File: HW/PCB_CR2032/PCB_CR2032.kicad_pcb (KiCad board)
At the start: 4 copper layers, 39.1 x 48 mm, 76 parts, among them J1 STDC14, J2 Breakoff, J3 PWR, M00 LED, M01 LED, M02 LED, M03 LED, M10 LED, M11 LED, M12 LED, M13 LED, SW1 WAKE, U1 STM32L071CBTx, U2 LIS3DH, Y1 32768 Hz

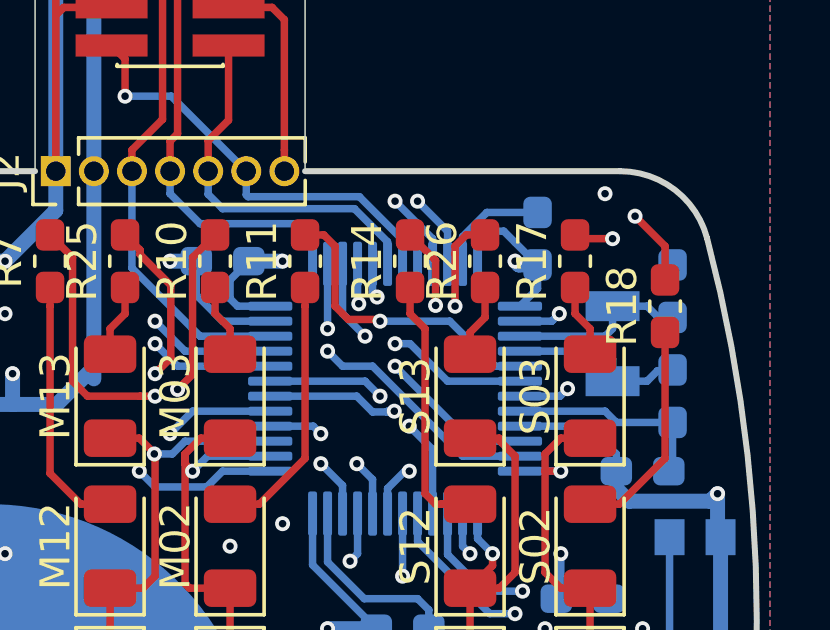
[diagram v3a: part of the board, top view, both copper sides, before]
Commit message: Connected BOOT0 pin to GND after forst board bring up.
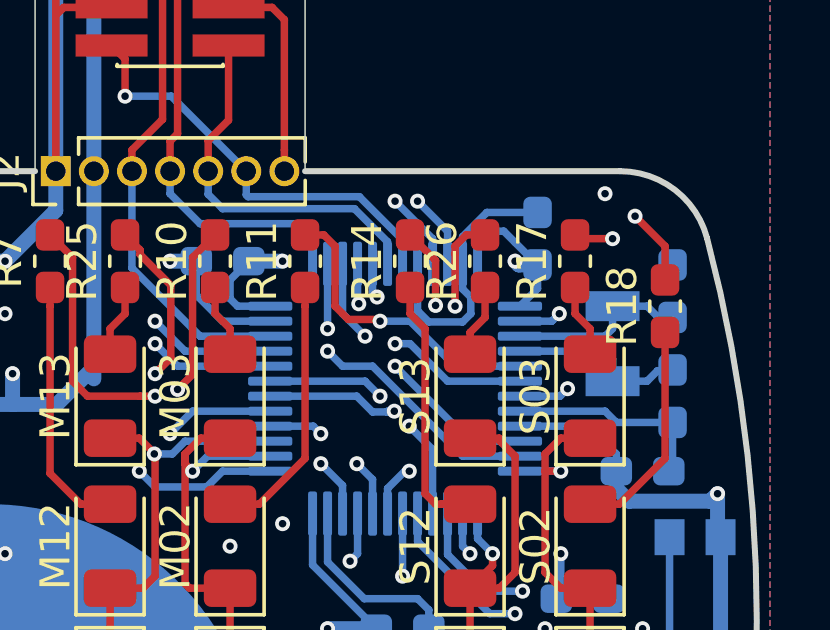
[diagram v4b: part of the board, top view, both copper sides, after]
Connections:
- U1 pad 44: Net-(U1-Pad44) -> GND
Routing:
- net GND: track 105.1 -> 110.4 mm
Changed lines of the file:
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@@
     (thickness 1.6)
     (drawings 14)
-    (tracks 762)
+    (tracks 769)
     (zones 0)
     (modules 76)
-    (nets 84)
+    (nets 83)
   )
   (page A4)
@@
   (net 73 /LED/LED_S_0_DIM)
   (net 74 /LED/LED_S_1_DIM)
-  (net 75 "Net-(U1-Pad44)")
-  (net 76 "Net-(U2-Pad2)")
-  (net 77 "Net-(U2-Pad3)")
-  (net 78 "Net-(U2-Pad7)")
-  (net 79 "Net-(U2-Pad13)")
-  (net 80 "Net-(U2-Pad15)")
-  (net 81 "Net-(U2-Pad16)")
-  (net 82 "Net-(D3-Pad2)")
-  (net 83 "Net-(D3-Pad1)")
+  (net 75 "Net-(U2-Pad2)")
+  (net 76 "Net-(U2-Pad3)")
+  (net 77 "Net-(U2-Pad7)")
+  (net 78 "Net-(U2-Pad13)")
+  (net 79 "Net-(U2-Pad15)")
+  (net 80 "Net-(U2-Pad16)")
+  (net 81 "Net-(D3-Pad2)")
+  (net 82 "Net-(D3-Pad1)")
   (net_class Default "This is the default net class."
     (clearance 0.15)
@@
     (add_net "Net-(R20-Pad1)")
     (add_net "Net-(R26-Pad1)")
-    (add_net "Net-(U1-Pad44)")
     (add_net "Net-(U2-Pad13)")
     (add_net "Net-(U2-Pad15)")
@@
       (net 29 /Debug/DBG_RX))
     (pad 44 smd roundrect (at -0.75 4.1625 180) (size 0.3 1.475) (layers B.Cu B.Paste B.Mask) (roundrect_rratio 0.25)
-      (net 75 "Net-(U1-Pad44)"))
+      (net 2 GND))
     (pad 45 smd roundrect (at -1.25 4.1625 180) (size 0.3 1.475) (layers B.Cu B.Paste B.Mask) (roundrect_rratio 0.25)
       (net 44 /LED/LED_H_02))
@@
       (net 5 VDD))
     (pad 2 smd roundrect (at -1.225 0.5) (size 0.55 0.35) (layers B.Cu B.Paste B.Mask) (roundrect_rratio 0.25)
-      (net 76 "Net-(U2-Pad2)"))
+      (net 75 "Net-(U2-Pad2)"))
     (pad 3 smd roundrect (at -1.225 0) (size 0.55 0.35) (layers B.Cu B.Paste B.Mask) (roundrect_rratio 0.25)
-      (net 77 "Net-(U2-Pad3)"))
+      (net 76 "Net-(U2-Pad3)"))
     (pad 4 smd roundrect (at -1.225 -0.5) (size 0.55 0.35) (layers B.Cu B.Paste B.Mask) (roundrect_rratio 0.25)
       (net 72 /MCU/ACC_SCL))
@@
       (net 71 /MCU/ACC_SDA))
     (pad 7 smd roundrect (at 0 -1.225) (size 0.35 0.55) (layers B.Cu B.Paste B.Mask) (roundrect_rratio 0.25)
-      (net 78 "Net-(U2-Pad7)"))
+      (net 77 "Net-(U2-Pad7)"))
     (pad 8 smd roundrect (at 0.5 -1.225) (size 0.35 0.55) (layers B.Cu B.Paste B.Mask) (roundrect_rratio 0.25)
       (net 5 VDD))
     (pad 9 smd roundrect (at 1.225 -1) (size 0.55 0.35) (layers B.Cu B.Paste B.Mask) (roundrect_rratio 0.25)
-      (net 83 "Net-(D3-Pad1)"))
+      (net 82 "Net-(D3-Pad1)"))
     (pad 10 smd roundrect (at 1.225 -0.5) (size 0.55 0.35) (layers B.Cu B.Paste B.Mask) (roundrect_rratio 0.25)
       (net 2 GND))
     (pad 11 smd roundrect (at 1.225 0) (size 0.55 0.35) (layers B.Cu B.Paste B.Mask) (roundrect_rratio 0.25)
-      (net 82 "Net-(D3-Pad2)"))
+      (net 81 "Net-(D3-Pad2)"))
     (pad 12 smd roundrect (at 1.225 0.5) (size 0.55 0.35) (layers B.Cu B.Paste B.Mask) (roundrect_rratio 0.25)
       (net 2 GND))
     (pad 13 smd roundrect (at 1.225 1) (size 0.55 0.35) (layers B.Cu B.Paste B.Mask) (roundrect_rratio 0.25)
-      (net 79 "Net-(U2-Pad13)"))
+      (net 78 "Net-(U2-Pad13)"))
     (pad 14 smd roundrect (at 0.5 1.225) (size 0.35 0.55) (layers B.Cu B.Paste B.Mask) (roundrect_rratio 0.25)
       (net 5 VDD))
     (pad 15 smd roundrect (at 0 1.225) (size 0.35 0.55) (layers B.Cu B.Paste B.Mask) (roundrect_rratio 0.25)
-      (net 80 "Net-(U2-Pad15)"))
+      (net 79 "Net-(U2-Pad15)"))
     (pad 16 smd roundrect (at -0.5 1.225) (size 0.35 0.55) (layers B.Cu B.Paste B.Mask) (roundrect_rratio 0.25)
-      (net 81 "Net-(U2-Pad16)"))
+      (net 80 "Net-(U2-Pad16)"))
     (model ${KISYS3DMOD}/Package_LGA.3dshapes/LGA-16_3x3mm_P0.5mm_LayoutBorder3x5y.wrl
       (at (xyz 0 0 0))
@@
       (net 11 /Accelerometer/WAKE_UP))
     (pad 2 smd rect (at -1.5 -0.95) (size 1.9 0.8) (layers B.Cu B.Paste B.Mask)
-      (net 82 "Net-(D3-Pad2)"))
+      (net 81 "Net-(D3-Pad2)"))
     (pad 1 smd rect (at -1.5 0.95) (size 1.9 0.8) (layers B.Cu B.Paste B.Mask)
-      (net 83 "Net-(D3-Pad1)"))
+      (net 82 "Net-(D3-Pad1)"))
     (model ${KISYS3DMOD}/Package_TO_SOT_SMD.3dshapes/SOT-23.wrl
       (at (xyz 0 0 0))
@@
   (gr_arc (start 119.55773 100) (end 167.900571 112.765957) (angle -29.58499408) (layer Edge.Cuts) (width 0.2))
   (gr_line (start 165 115) (end 135.000001 115) (layer Edge.Cuts) (width 0.2))
-  (via (at 147 111.25) (size 0.5) (drill 0.25) (layers F.Cu B.Cu) (net 2))
-  (via (at 151.25 107.5) (size 0.5) (drill 0.25) (layers F.Cu B.Cu) (net 2))
-  (via (at 137.75 99.25) (size 0.5) (drill 0.25) (layers F.Cu B.Cu) (net 2))
-  (via (at 144.5 97.75) (size 0.5) (drill 0.25) (layers F.Cu B.Cu) (net 2))
   (segment (start 132.55 97.425) (end 132.5 97.375) (width 0.5) (layer B.Cu) (net 1))
   (segment (start 132.55 105) (end 132.55 97.425) (width 0.5) (layer B.Cu) (net 1))
@@
   (segment (start 133.625 97.375) (end 132.5 97.375) (width 0.5) (layer B.Cu) (net 1))
   (segment (start 134.5 96.5) (end 133.625 97.375) (width 0.5) (layer B.Cu) (net 1))
+  (via (at 147 111.25) (size 0.5) (drill 0.25) (layers F.Cu B.Cu) (net 2))
+  (via (at 151.25 107.5) (size 0.5) (drill 0.25) (layers F.Cu B.Cu) (net 2))
+  (via (at 137.75 99.25) (size 0.5) (drill 0.25) (layers F.Cu B.Cu) (net 2))
+  (via (at 144.5 97.75) (size 0.5) (drill 0.25) (layers F.Cu B.Cu) (net 2))
   (segment (start 146.19 85) (end 146.19 79.81) (width 0.25) (layer F.Cu) (net 2))
   (segment (start 146.46 79.54) (end 148.05 79.54) (width 0.25) (layer F.Cu) (net 2))
@@
   (via (at 165.75 100.25) (size 0.5) (drill 0.25) (layers F.Cu B.Cu) (net 2))
   (via (at 164.5 85.75) (size 0.5) (drill 0.25) (layers F.Cu B.Cu) (net 2))
+  (segment (start 159.75 88.925) (end 159.75 88.0875) (width 0.25) (layer B.Cu) (net 2))
+  (segment (start 160.025001 89.200001) (end 159.75 88.925) (width 0.25) (layer B.Cu) (net 2))
+  (segment (start 159.752001 90.025001) (end 160.025001 89.752001) (width 0.25) (layer B.Cu) (net 2))
+  (segment (start 160.025001 89.752001) (end 160.025001 89.200001) (width 0.25) (layer B.Cu) (net 2))
+  (segment (start 158.622996 90.025001) (end 159.752001 90.025001) (width 0.25) (layer B.Cu) (net 2))
+  (segment (start 158.25 89.652005) (end 158.622996 90.025001) (width 0.25) (layer B.Cu) (net 2))
+  (segment (start 158.25 88.0875) (end 158.25 89.652005) (width 0.25) (layer B.Cu) (net 2))
   (segment (start 165.9 89.5) (end 166.25 89.85) (width 0.25) (layer B.Cu) (net 3))
   (segment (start 164.75 89.5) (end 165.9 89.5) (width 0.25) (layer B.Cu) (net 3))
@@
   (segment (start 158 90.75) (end 159.25 92) (width 0.25) (layer B.Cu) (net 50))
   (via (at 157 90) (size 0.5) (drill 0.25) (layers F.Cu B.Cu) (net 51))
-  (segment (start 159.325 90) (end 157 90) (width 0.25) (layer B.Cu) (net 51))
-  (segment (start 161.6625 91.5) (end 160.825 91.5) (width 0.25) (layer B.Cu) (net 51))
-  (segment (start 160.825 91.5) (end 159.325 90) (width 0.25) (layer B.Cu) (net 51))
   (segment (start 155.943621 89.943621) (end 155.5 89.5) (width 0.25) (layer F.Cu) (net 51))
   (segment (start 157 90) (end 156.94362 89.943621) (width 0.25) (layer F.Cu) (net 51))
@@
   (segment (start 155.125 87.125) (end 154.5 87.125) (width 0.25) (layer F.Cu) (net 51))
   (segment (start 155.5 87.5) (end 155.125 87.125) (width 0.25) (layer F.Cu) (net 51))
+  (segment (start 158 90) (end 157 90) (width 0.25) (layer B.Cu) (net 51))
+  (segment (start 161.6625 91.5) (end 159.5 91.5) (width 0.25) (layer B.Cu) (net 51))
+  (segment (start 159.5 91.5) (end 158 90) (width 0.25) (layer B.Cu) (net 51))
   (via (at 155.025 93.75) (size 0.5) (drill 0.25) (layers F.Cu B.Cu) (net 52))
   (segment (start 153.3375 93.5) (end 154.775 93.5) (width 0.25) (layer B.Cu) (net 52))
@@
   (segment (start 160.75 98.15) (end 160 98.9) (width 0.25) (layer F.Cu) (net 74))
   (segment (start 160.75 97.75) (end 160.75 98.15) (width 0.25) (layer F.Cu) (net 74))
-  (segment (start 165.45 104.55) (end 164.25 104.55) (width 0.25) (layer B.Cu) (net 82))
-  (segment (start 165.75 104.85) (end 165.45 104.55) (width 0.25) (layer B.Cu) (net 82))
-  (segment (start 165.75 108.125) (end 165.75 104.85) (width 0.25) (layer B.Cu) (net 82))
-  (segment (start 164.375 109.5) (end 165.75 108.125) (width 0.25) (layer B.Cu) (net 82))
-  (segment (start 164 109.5) (end 164.375 109.5) (width 0.25) (layer B.Cu) (net 82))
-  (segment (start 164 106.7) (end 164.25 106.45) (width 0.25) (layer B.Cu) (net 83))
-  (segment (start 164 108.5) (end 164 106.7) (width 0.25) (layer B.Cu) (net 83))
+  (segment (start 165.45 104.55) (end 164.25 104.55) (width 0.25) (layer B.Cu) (net 81))
+  (segment (start 165.75 104.85) (end 165.45 104.55) (width 0.25) (layer B.Cu) (net 81))
+  (segment (start 165.75 108.125) (end 165.75 104.85) (width 0.25) (layer B.Cu) (net 81))
+  (segment (start 164.375 109.5) (end 165.75 108.125) (width 0.25) (layer B.Cu) (net 81))
+  (segment (start 164 109.5) (end 164.375 109.5) (width 0.25) (layer B.Cu) (net 81))
+  (segment (start 164 106.7) (end 164.25 106.45) (width 0.25) (layer B.Cu) (net 82))
+  (segment (start 164 108.5) (end 164 106.7) (width 0.25) (layer B.Cu) (net 82))
   (zone (net 2) (net_name GND) (layer B.Cu) (hatch edge 0.508)
     (connect_pads (clearance 0.25))

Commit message: Ordered V2.0 PCB
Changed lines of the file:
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@@
     (solder_mask_min_width 0.25)
     (aux_axis_origin 0 0)
-    (visible_elements 7FFFFFFF)
+    (visible_elements 7FFF7FFF)
     (pcbplotparams
       (layerselection 0x010fc_ffffffff)
@@
       (outputformat 1)
       (mirror false)
-      (drillshape 1)
+      (drillshape 0)
       (scaleselection 1)
-      (outputdirectory ""))
+      (outputdirectory "order_v2.0/"))
   )
   (net 0 "")
@@
     (tags "capacitor handsolder")
     (attr smd)
-    (fp_text reference C1 (at 0 1.43 90) (layer B.SilkS)
+    (fp_text reference C1 (at 1 -1.75 180) (layer B.SilkS)
       (effects (font (size 1 1) (thickness 0.15)) (justify mirror))
     )
@@
     (tags "capacitor handsolder")
     (attr smd)
-    (fp_text reference C2 (at 0 1.43 90) (layer B.SilkS)
+    (fp_text reference C2 (at 1 1.75 180) (layer B.SilkS)
       (effects (font (size 1 1) (thickness 0.15)) (justify mirror))
     )
@@
     (tags "capacitor handsolder")
     (attr smd)
-    (fp_text reference C3 (at 0 1.65 270) (layer B.SilkS)
+    (fp_text reference C3 (at -2.75 0) (layer B.SilkS)
       (effects (font (size 1 1) (thickness 0.15)) (justify mirror))
     )
@@
     (tags "capacitor handsolder")
     (attr smd)
-    (fp_text reference C5 (at 0 1.43) (layer B.SilkS)
+    (fp_text reference C5 (at -0.75 1.43) (layer B.SilkS)
       (effects (font (size 1 1) (thickness 0.15)) (justify mirror))
     )
@@
     (tags "capacitor handsolder")
     (attr smd)
-    (fp_text reference C6 (at 0 1.43 90) (layer B.SilkS)
+    (fp_text reference C6 (at 1 2 180) (layer B.SilkS)
       (effects (font (size 1 1) (thickness 0.15)) (justify mirror))
     )
@@
     (tags "capacitor handsolder")
     (attr smd)
-    (fp_text reference C9 (at 0 1.43) (layer B.SilkS)
+    (fp_text reference C9 (at 0 -1.5) (layer B.SilkS)
       (effects (font (size 1 1) (thickness 0.15)) (justify mirror))
     )
@@
     (tags "capacitor handsolder")
     (attr smd)
-    (fp_text reference C13 (at 0 1.65 270) (layer B.SilkS)
+    (fp_text reference C13 (at -2.75 0) (layer B.SilkS)
       (effects (font (size 1 1) (thickness 0.15)) (justify mirror))
     )
@@
     (tags "capacitor handsolder")
     (attr smd)
-    (fp_text reference C15 (at 0 1.43 90) (layer B.SilkS)
+    (fp_text reference C15 (at 3.25 1.75 90) (layer B.SilkS)
       (effects (font (size 1 1) (thickness 0.15)) (justify mirror))
     )
@@
     (tags "resistor handsolder")
     (attr smd)
-    (fp_text reference R1 (at -0.171267 -1.49 90) (layer F.SilkS)
+    (fp_text reference R1 (at -3 1.5 90) (layer F.SilkS)
       (effects (font (size 1 1) (thickness 0.15)))
     )
@@
     (tags "resistor handsolder")
     (attr smd)
-    (fp_text reference R18 (at 0 -1.43 90) (layer F.SilkS)
+    (fp_text reference R18 (at -3 1.5 90) (layer F.SilkS)
       (effects (font (size 1 1) (thickness 0.15)))
     )
@@
     (tags "resistor handsolder")
     (attr smd)
-    (fp_text reference R19 (at 0 -1.43 90) (layer F.SilkS)
+    (fp_text reference R19 (at -3 -1.5 90) (layer F.SilkS)
       (effects (font (size 1 1) (thickness 0.15)))
     )
@@
     (tags "resistor handsolder")
     (attr smd)
-    (fp_text reference R24 (at 0 -1.43 90) (layer F.SilkS)
+    (fp_text reference R24 (at -3 -1.5 90) (layer F.SilkS)
       (effects (font (size 1 1) (thickness 0.15)))
     )
@@
     (tags "resistor handsolder")
     (attr smd)
-    (fp_text reference R27 (at 0 1.43 90) (layer B.SilkS)
+    (fp_text reference R27 (at -3.25 0.25 90) (layer B.SilkS)
       (effects (font (size 1 1) (thickness 0.15)) (justify mirror))
     )
@@
     (tags "resistor handsolder")
     (attr smd)
-    (fp_text reference R28 (at 0 1.43 90) (layer B.SilkS)
+    (fp_text reference R28 (at 3.25 2 90) (layer B.SilkS)
       (effects (font (size 1 1) (thickness 0.15)) (justify mirror))
     )
@@
     (tags "resistor handsolder")
     (attr smd)
-    (fp_text reference R29 (at 0 1.43 90) (layer B.SilkS)
+    (fp_text reference R29 (at 3.375 0 90) (layer B.SilkS)
       (effects (font (size 1 1) (thickness 0.15)) (justify mirror))
     )
@@
     (tags "resistor handsolder")
     (attr smd)
-    (fp_text reference R30 (at 0 1.43 90) (layer B.SilkS)
+    (fp_text reference R30 (at -3.25 -2.25 90) (layer B.SilkS)
       (effects (font (size 1 1) (thickness 0.15)) (justify mirror))
     )
@@
     (tags "resistor handsolder")
     (attr smd)
-    (fp_text reference R31 (at 0 1.43 90) (layer B.SilkS)
+    (fp_text reference R31 (at 3.125 0 90) (layer B.SilkS)
       (effects (font (size 1 1) (thickness 0.15)) (justify mirror))
     )
@@
   (module "BCD-watch:WS-TASU SMT Tact Switch" (layer B.Cu)
     (at 167.5 100 270)
-    (fp_text reference SW1 (at 0 2.54 90) (layer B.SilkS)
+    (fp_text reference SW1 (at -5 -0.75 270) (layer B.SilkS)
       (effects (font (size 1 1) (thickness 0.15)) (justify mirror))
     )
@@
     (tags "LGA NoLead")
     (attr smd)
-    (fp_text reference U2 (at 0 2.45) (layer B.SilkS)
+    (fp_text reference U2 (at 2.725 0.75 90) (layer B.SilkS)
       (effects (font (size 1 1) (thickness 0.15)) (justify mirror))
     )
@@
   (module BCD-watch:FC-135 (layer B.Cu)
     (at 164.75 90.75 270)
-    (fp_text reference Y1 (at 0 2.54 90) (layer B.SilkS)
+    (fp_text reference Y1 (at 0 1.5 90) (layer B.SilkS)
       (effects (font (size 1 1) (thickness 0.15)) (justify mirror))
     )
@@
     (descr "Through hole straight pin header, 1x07, 1.27mm pitch, single row")
     (tags "Through hole pin header THT 1x07 1.27mm single row")
-    (fp_text reference J2 (at 0 -1.695 90) (layer F.SilkS)
+    (fp_text reference J2 (at 2.25 3.81 180) (layer F.SilkS)
       (effects (font (size 1 1) (thickness 0.15)))
     )
@@
   (module BCD-watch:BAT-HLD-001-xx-OTL (layer B.Cu)
     (at 144 105 180)
-    (fp_text reference BT1 (at -6.35 10.16) (layer B.SilkS)
-      (effects (font (size 1 1) (thickness 0.15)) (justify mirror))
-    )
+    (fp_text reference BT1 (at -6.35 10.16) (layer B.SilkS) hide
+      (effects (font (size 1 1) (thickness 0.15)) (justify mirror))
+    )
